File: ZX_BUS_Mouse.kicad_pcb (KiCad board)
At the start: 2 copper layers, 99.1 x 99.1 mm, 37 parts, among them J1 X1A, J2 X1B, J3 Conn_02x30_Odd_Even

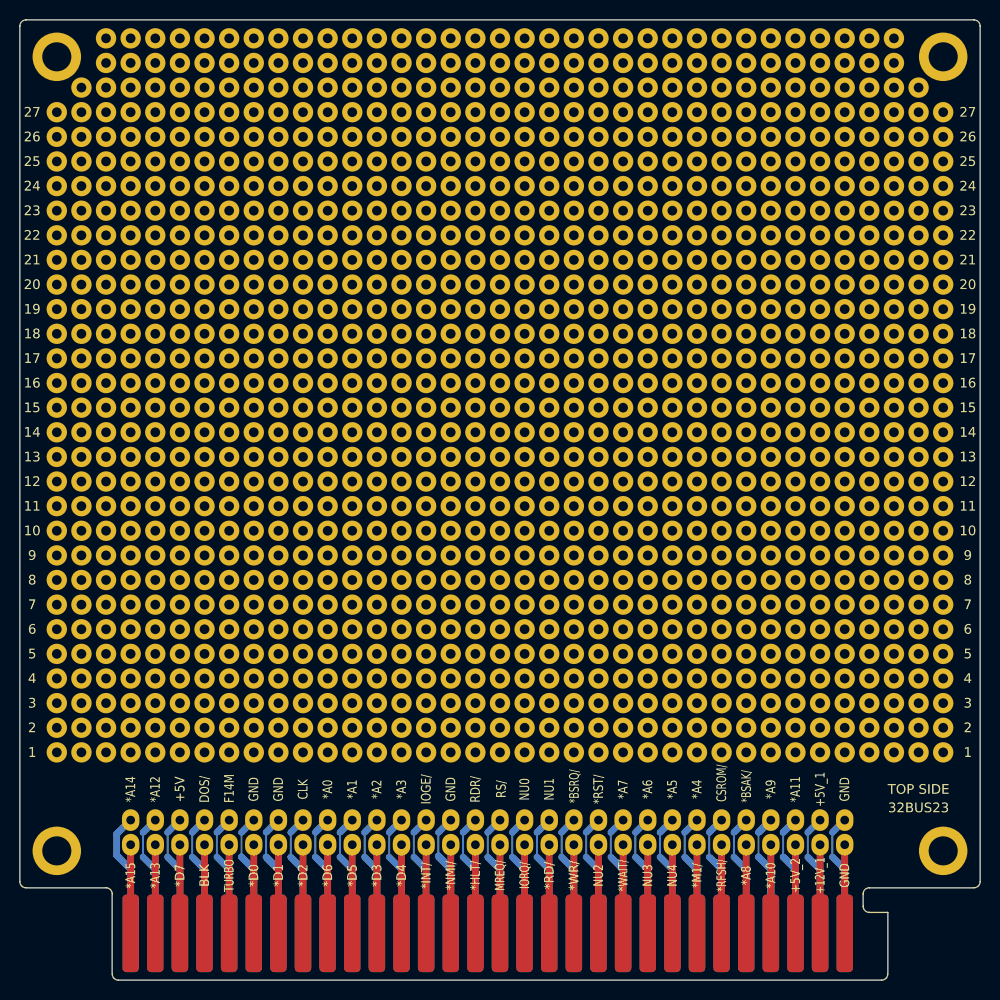
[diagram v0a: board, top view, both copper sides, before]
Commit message: Route PCB. Reassign EPM3032 IO pins.
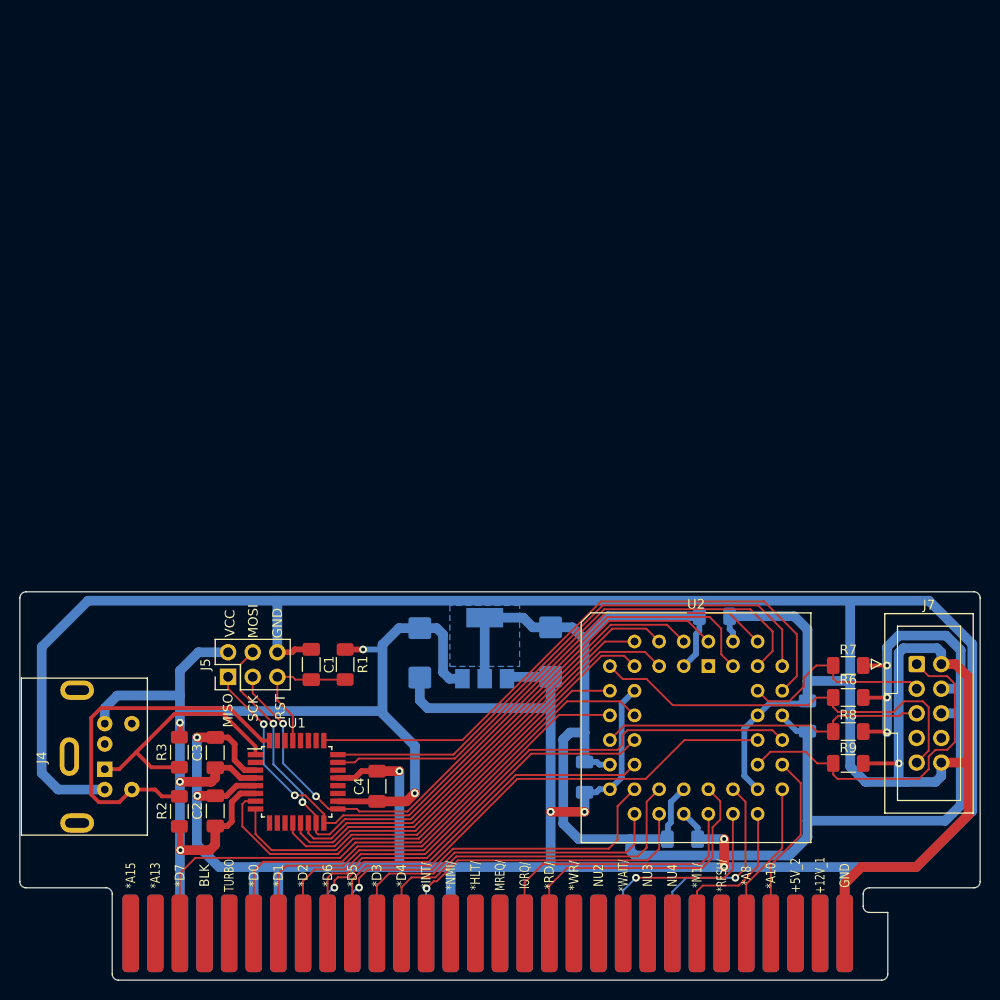
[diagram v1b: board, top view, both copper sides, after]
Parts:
- removed J3: Conn_02x30_Odd_Even, my_lib:PinSocket_2x30_P2.54mm_Vertical
- removed REF** (x27): holes1, my_lib:holes1
- removed REF** (x4): hole_5mm, my_lib:hole_5mm
- removed REF**: holes2, my_lib:holes2
- removed REF** (x2): holes3, my_lib:holes3
- added C1: 0.1u, Capacitor_SMD:C_1206_3216Metric_Pad1.33x1.80mm_HandSolder, F.Cu at (72.6, 117.3)
- added C10: 22u, Capacitor_Tantalum_SMD:CP_EIA-6032-28_Kemet-C_Pad2.25x2.35mm_HandSolder, B.Cu at (97.3, 116.0)
- added C2: 0.1u, Capacitor_SMD:C_1206_3216Metric_Pad1.33x1.80mm_HandSolder, F.Cu at (62.7, 132.4)
- added C3: 0.1u, Capacitor_SMD:C_1206_3216Metric_Pad1.33x1.80mm_HandSolder, F.Cu at (62.7, 126.4)
- added C4: 0.1u, Capacitor_SMD:C_1206_3216Metric_Pad1.33x1.80mm_HandSolder, F.Cu at (79.4, 129.9)
- added C5: 0.1u, Capacitor_SMD:C_1206_3216Metric_Pad1.33x1.80mm_HandSolder, B.Cu at (123.8, 122.6)
- added C6: 0.1u, Capacitor_SMD:C_1206_3216Metric_Pad1.33x1.80mm_HandSolder, B.Cu at (114.2, 112.3)
- added C7: 0.1u, Capacitor_SMD:C_1206_3216Metric_Pad1.33x1.80mm_HandSolder, B.Cu at (110.9, 135.3)
- added C8: 0.1u, Capacitor_SMD:C_1206_3216Metric_Pad1.33x1.80mm_HandSolder, B.Cu at (100.8, 128.9)
- added C9: 10u, Capacitor_Tantalum_SMD:CP_EIA-6032-28_Kemet-C_Pad2.25x2.35mm_HandSolder, B.Cu at (83.8, 116.1)
- added J4: Mini-DIN-6, Connector_Mini-DIN_Female_6Pin:Connector_Mini-DIN_Female_6Pin_2rows, F.Cu at (51.3, 128.1)
- added J5: Conn_02x03_Odd_Even ISP, Connector_PinHeader_2.54mm:PinHeader_2x03_P2.54mm_Vertical, F.Cu at (64.0, 118.6)
- added J7: Conn_02x05_Odd_Even JTAG, Connector_IDC:IDC-Header_2x05_P2.54mm_Vertical, F.Cu at (135.1, 117.3)
- added R1: 2.2K, Resistor_SMD:R_1206_3216Metric_Pad1.30x1.75mm_HandSolder, F.Cu at (76.1, 117.3)
- added R2: 4.7K, Resistor_SMD:R_1206_3216Metric_Pad1.30x1.75mm_HandSolder, F.Cu at (59.0, 132.4)
- added R3: 4.7K, Resistor_SMD:R_1206_3216Metric_Pad1.30x1.75mm_HandSolder, F.Cu at (59.0, 126.3)
- added R6: 10K, Resistor_SMD:R_1206_3216Metric_Pad1.30x1.75mm_HandSolder, F.Cu at (128.0, 120.7)
- added R7: 10K, Resistor_SMD:R_1206_3216Metric_Pad1.30x1.75mm_HandSolder, F.Cu at (128.0, 117.4)
- added R8: 10K, Resistor_SMD:R_1206_3216Metric_Pad1.30x1.75mm_HandSolder, F.Cu at (128.0, 124.2)
- added R9: 10K, Resistor_SMD:R_1206_3216Metric_Pad1.30x1.75mm_HandSolder, F.Cu at (128.0, 127.5)
- added U1: ATmega8A-A, Package_QFP:TQFP-32_7x7mm_P0.8mm, F.Cu at (71.1, 129.4)
- added U2: EPM3032ALC44, Package_LCC:PLCC-44_THT-Socket, F.Cu at (113.6, 117.5)
- added U3: AMS1117-3.3, Package_TO_SOT_SMD:SOT-223-3_TabPin2, B.Cu at (90.5, 115.6)
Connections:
- net /GND renamed GND
- J1 pad 3: /+5V -> VCC
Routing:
- net GND: track 105.8 -> 497.9 mm, vias 0 -> 8
- net /+3.3V: track 0.00 -> 176.1 mm, vias 0 -> 3
- net VCC: track 0.00 -> 131.4 mm, vias 0 -> 5
- net /DI4/MISO: track 0.00 -> 74.5 mm, vias 0 -> 2
- net /DI3/MOSI: track 0.00 -> 72.9 mm, vias 0 -> 2
- net /DI5/SCK: track 0.00 -> 71.1 mm, vias 0 -> 2
- net /MKEY: track 0.00 -> 62.5 mm
- net /MY: track 0.00 -> 57.0 mm
- net /MX: track 0.00 -> 56.6 mm
- net /DI6: track 0.00 -> 54.3 mm
- net /DI7: track 0.00 -> 54.0 mm
- net /*D2: track 9.14 -> 62.3 mm
- net /DI2: track 0.00 -> 49.9 mm
- net /*D7: track 9.14 -> 58.3 mm
- net /DI1: track 0.00 -> 48.1 mm
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- added copper zone on B.Cu, net /+3.3V
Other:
- board size 99.1 x 99.1 mm -> 99.1 x 40.1 mm
- board text added: "MISO"
- board text added: "MOSI"
- board text added: "RST"
- board text added: "SCK"
- board text added: "VCC"
- board text removed: "*A0"
- board text removed: "*A1"
- board text removed: "*A11"
- board text removed: "*A12"
- board text removed: "*A14"
- board text removed: "*A2"
- board text removed: "*A3"
- board text removed: "*A4"
- board text removed: "*A5"
- board text removed: "*A6"
- board text removed: "*A7"
- board text removed: "*A9"
- board text removed: "*BSAK/"
- board text removed: "*BSRQ/"
- board text removed: "*RST/"
- board text removed: "+5V"
- board text removed: "+5V_1"
- board text removed: "1"
- board text removed: "10"
- board text removed: "11"
- board text removed: "12"
- board text removed: "13"
- board text removed: "14"
- board text removed: "15"
- board text removed: "16"
- board text removed: "17"
- board text removed: "18"
- board text removed: "19"
- board text removed: "2"
- board text removed: "20"
- board text removed: "21"
- board text removed: "22"
- board text removed: "23"
- board text removed: "24"
- board text removed: "25"
- board text removed: "26"
- board text removed: "27"
- board text removed: "3"
- board text removed: "32BUS23"
- board text removed: "4"
- board text removed: "5"
- board text removed: "6"
- board text removed: "7"
- board text removed: "8"
- board text removed: "9"
- board text removed: "CLK"
- board text removed: "CSROM/"
- board text removed: "DOS/"
- board text removed: "F14M"
- board text removed: "IOGE/"
- board text removed: "NU0"
- board text removed: "NU1"
- board text removed: "RDR/"
- board text removed: "RS/"
- board text removed: "TOP SIDE"

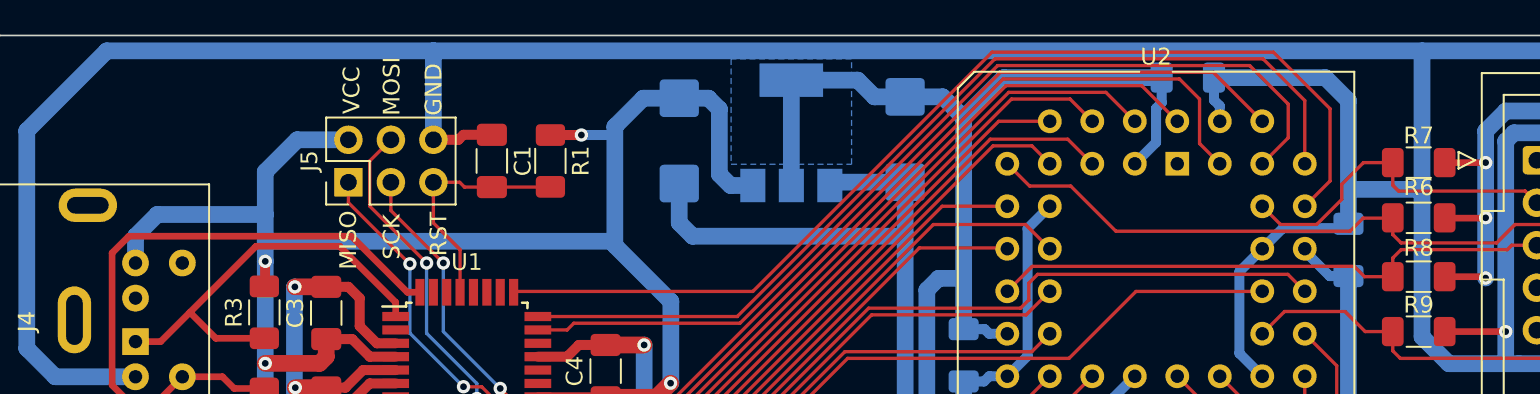
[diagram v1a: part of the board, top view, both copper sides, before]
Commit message: Add debug I2C connector on PCB. Disable solder mask on edge connector.
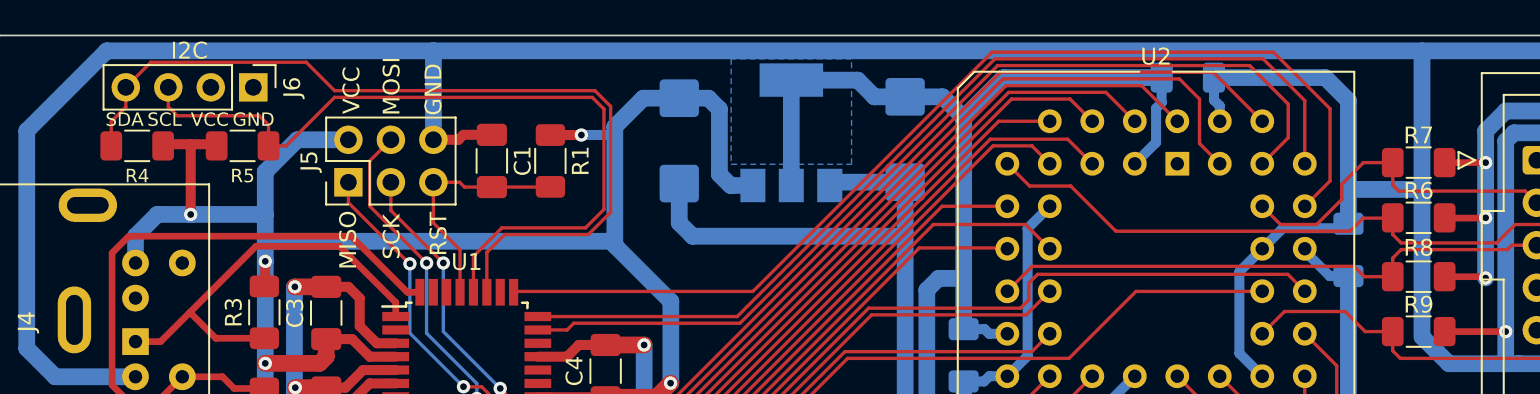
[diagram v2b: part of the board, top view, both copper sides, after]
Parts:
- added J6: Conn_01x04 Debug, Connector_PinHeader_2.54mm:PinHeader_1x04_P2.54mm_Vertical, F.Cu at (58.3, 112.9)
- added R4: 2.2K, Resistor_SMD:R_1206_3216Metric_Pad1.30x1.75mm_HandSolder, F.Cu at (51.4, 116.4)
- added R5: 2.2K, Resistor_SMD:R_1206_3216Metric_Pad1.30x1.75mm_HandSolder, F.Cu at (57.7, 116.4)
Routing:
- net /SDA: track 0.00 -> 51.7 mm
- net /SCL: track 0.00 -> 47.5 mm
- net VCC: track 131.4 -> 138.9 mm, vias 5 -> 6
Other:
- board text added: "I2C"
- board text added: "SCL"
- board text added: "SDA"

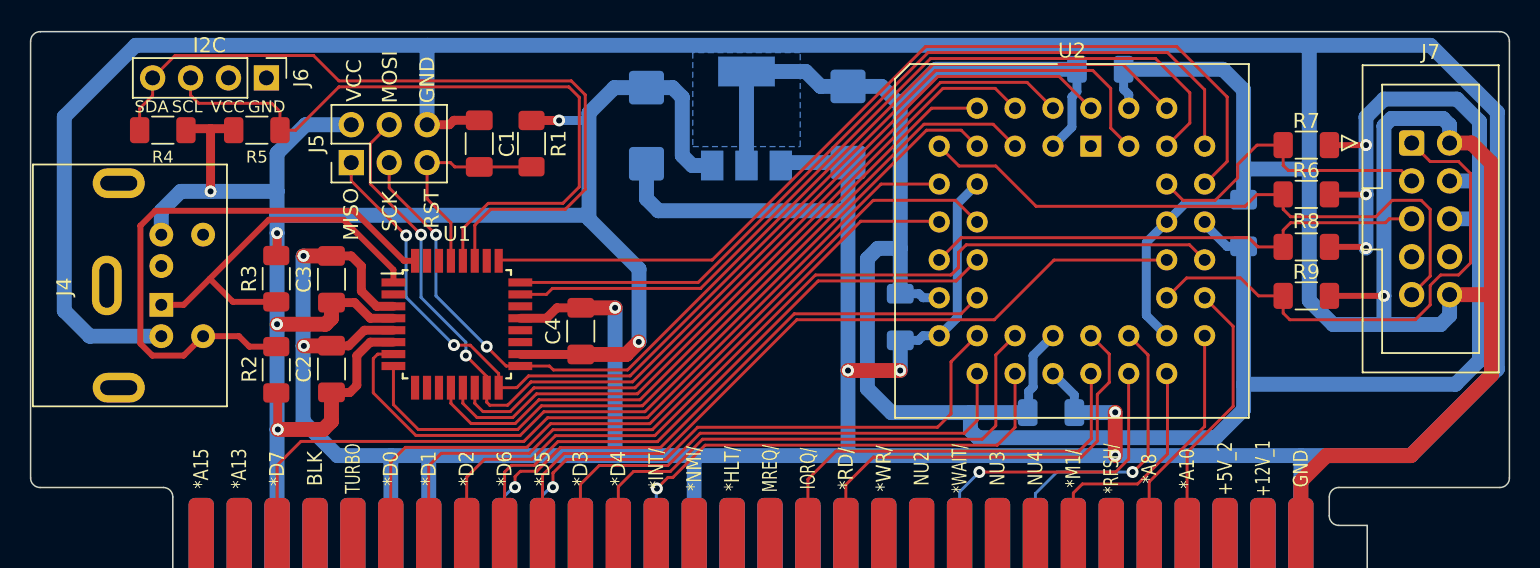
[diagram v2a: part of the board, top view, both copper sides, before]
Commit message: Board height 40 mm.
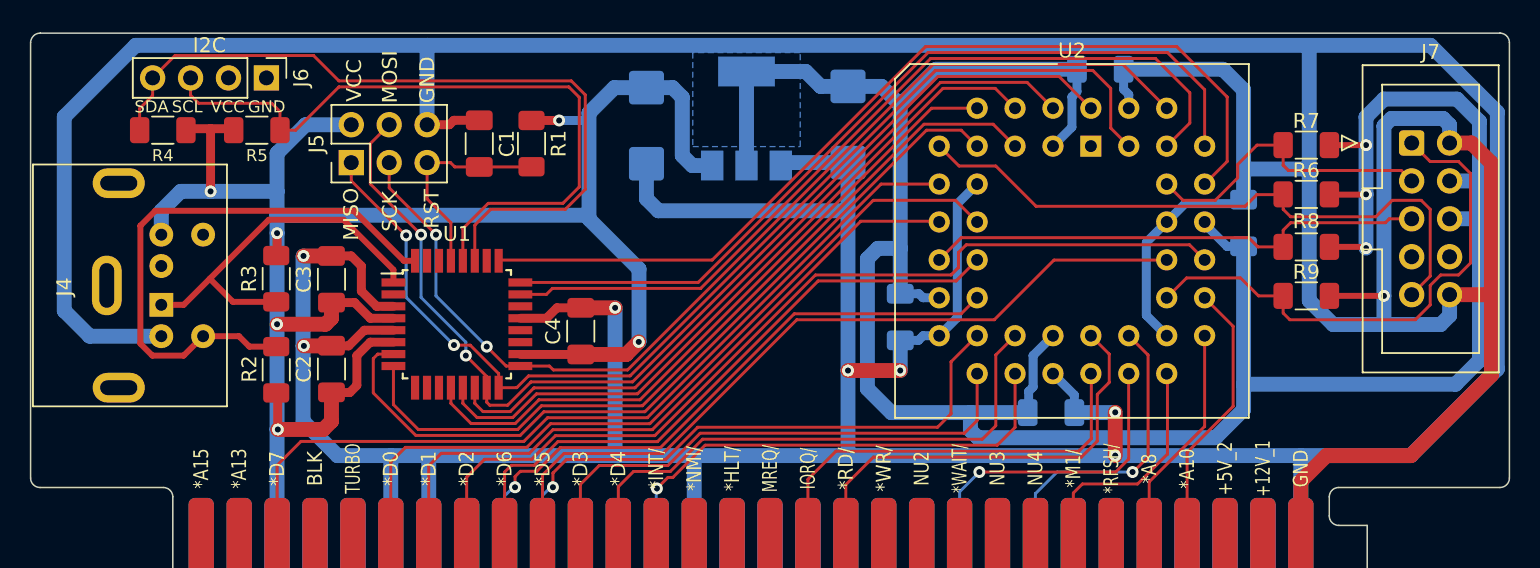
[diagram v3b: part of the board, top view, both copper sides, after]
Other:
- board size 99.1 x 40.1 mm -> 99.1 x 40 mm
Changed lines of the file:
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@@
     (property "ki_keywords" "R res resistor")
     (attr smd)
-    (fp_text reference "R4" (at 0 -1.8) (layer "F.SilkS")
+    (fp_text reference "R4" (at 0 -1.7) (layer "F.SilkS")
         (effects (font (size 0.8 0.8) (thickness 0.1)))
     )
@@
     (property "ki_keywords" "R res resistor")
     (attr smd)
-    (fp_text reference "R5" (at 0 1.8) (layer "F.SilkS")
+    (fp_text reference "R5" (at 0 1.7) (layer "F.SilkS")
         (effects (font (size 0.8 0.8) (thickness 0.1)))
     )
@@
     )
     (stroke (width 0.15) (type solid)) (fill solid) (layer "F.Mask"))
-  (gr_arc (start 42.545 110.435) (mid 42.740987 109.981845) (end 43.2 109.8)
+  (gr_arc (start 42.545 110.535) (mid 42.740987 110.081845) (end 43.2 109.9)
     (stroke (width 0.1) (type solid)) (layer "Edge.Cuts"))
   (gr_arc (start 129.54 140.97) (mid 129.725987 140.520987) (end 130.175 140.335)
     (stroke (width 0.1) (type solid)) (layer "Edge.Cuts"))
-  (gr_line (start 43.2 109.8) (end 140.97 109.8)
+  (gr_line (start 43.2 109.9) (end 140.97 109.9)
     (stroke (width 0.1) (type solid)) (layer "Edge.Cuts"))
   (gr_arc (start 52.705 149.86) (mid 52.255987 149.674013) (end 52.07 149.225)
@@
   (gr_arc (start 51.435 140.335) (mid 51.884013 140.520987) (end 52.07 140.97)
     (stroke (width 0.1) (type solid)) (layer "Edge.Cuts"))
-  (gr_line (start 42.545 139.7) (end 42.545 110.435)
+  (gr_line (start 42.545 139.7) (end 42.545 110.535)
     (stroke (width 0.1) (type solid)) (layer "Edge.Cuts"))
   (gr_arc (start 130.175 142.875) (mid 129.725987 142.689013) (end 129.54 142.24)
     (stroke (width 0.1) (type solid)) (layer "Edge.Cuts"))
-  (gr_arc (start 140.97 109.8) (mid 141.419013 109.985987) (end 141.605 110.435)
+  (gr_arc (start 140.97 109.9) (mid 141.419012 110.085987) (end 141.605 110.535)
     (stroke (width 0.1) (type solid)) (layer "Edge.Cuts"))
   (gr_line (start 52.07 149.225) (end 52.07 140.97)
     (stroke (width 0.1) (type solid)) (layer "Edge.Cuts"))
-  (gr_line (start 141.605 139.7) (end 141.605 110.435)
+  (gr_line (start 141.605 139.7) (end 141.605 110.535)
     (stroke (width 0.1) (type solid)) (layer "Edge.Cuts"))
   (gr_arc (start 132.08 149.225) (mid 131.894013 149.674013) (end 131.445 149.86)
